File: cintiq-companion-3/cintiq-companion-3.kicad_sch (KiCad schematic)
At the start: 8 parts, among them J3 13HD_buttonboard, J4 13HD_fingerpanel, X1 13HD_eDP, X2 13HD_penpanel

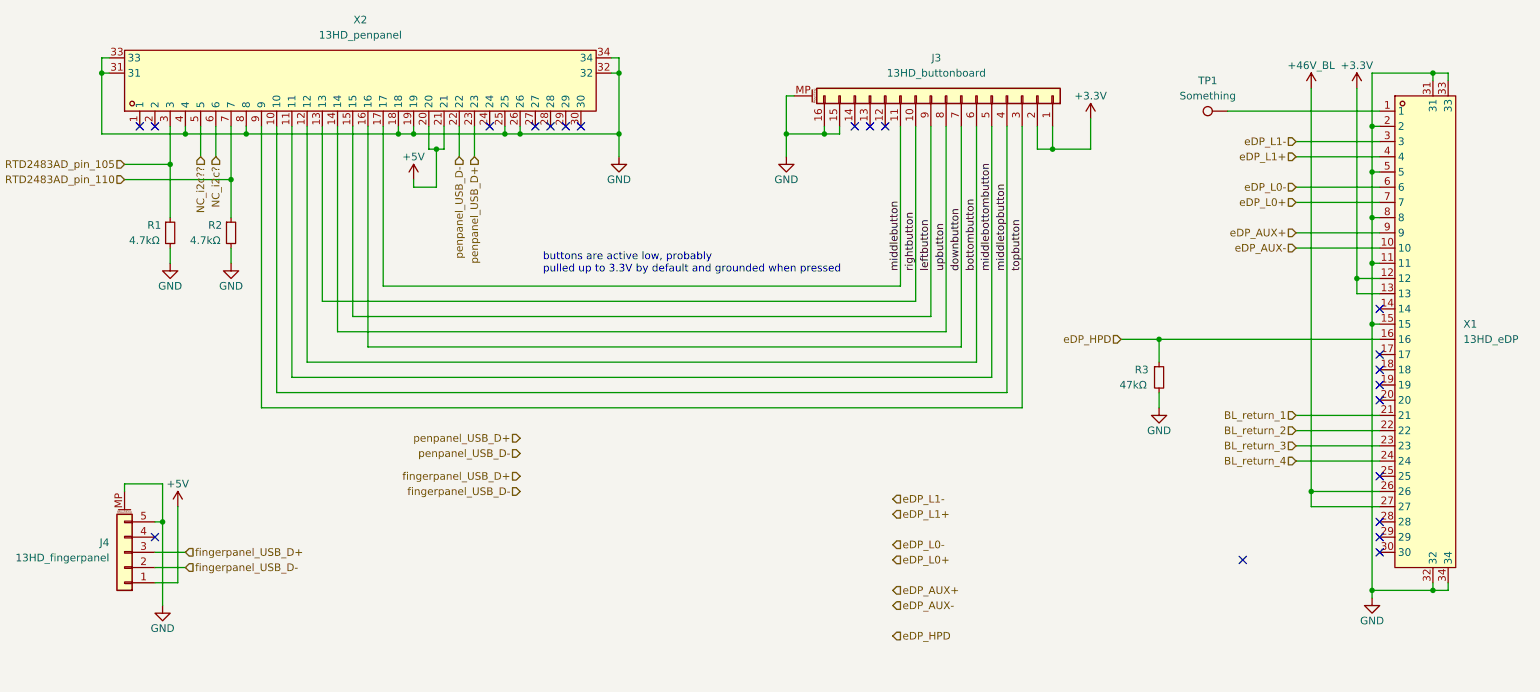
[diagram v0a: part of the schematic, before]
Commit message: Created PCB file with some footprints
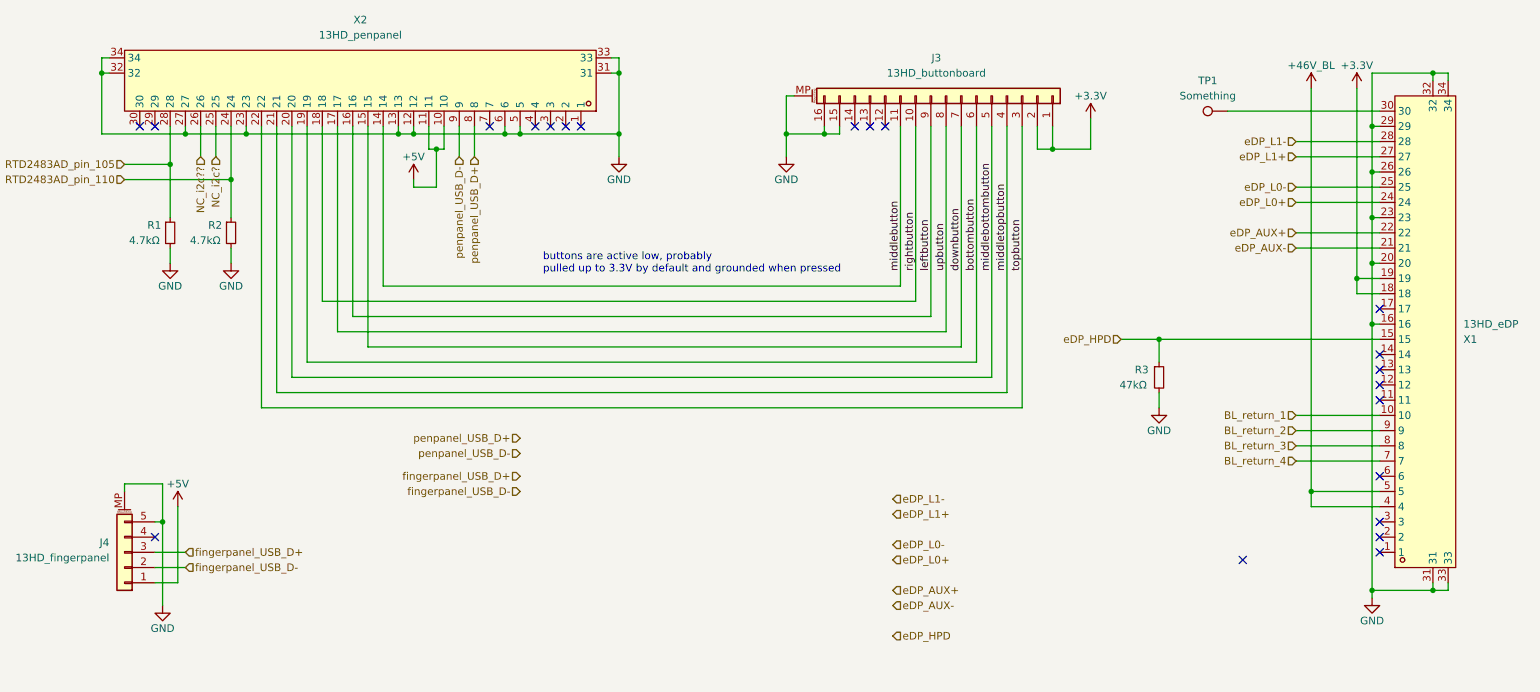
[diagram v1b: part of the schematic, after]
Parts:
- R1, R2, R3: footprint (none) -> Resistor_SMD:R_0603_1608Metric
- X1, X2: footprint 30pipex:FPC-SMD_ALC04-S30EIA-00 -> A_my_stuff:30pipex
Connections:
- net +3.3V: now also X1.18, X1.19; no longer X1.12, X1.13
- net +46V_BL: now also X1.4, X1.5; no longer X1.26, X1.27
- net +5V: now also X2.10, X2.11; no longer X2.20, X2.21
- net BL_return_1: now also X1.10; no longer X1.21
- net BL_return_2: now also X1.9; no longer X1.22
- net BL_return_3: now also X1.8; no longer X1.23
- net BL_return_4: now also X1.7; no longer X1.24
- net GND: now also X1.16, X1.20, X1.23, X1.26, X1.29, X2.12, X2.13, X2.23, X2.27, X2.5, X2.6; no longer X1.11, X1.15, X1.2, X1.5, X1.8, X2.18, X2.19, X2.25, X2.26, X2.4, X2.8
- net NC_i2c?: now also X2.25; no longer X2.6
- net NC_i2c??: now also X2.26; no longer X2.5
- net RTD2483AD_pin_105: now also X2.28; no longer X2.3
- net RTD2483AD_pin_110: now also X2.24; no longer X2.7
- net bottombutton: now also X2.19; no longer X2.12
- net downbutton: now also X2.15; no longer X2.16
- net eDP_AUX+: now also X1.22; no longer X1.9
- net eDP_AUX-: now also X1.21; no longer X1.10
- net eDP_HPD: now also X1.15; no longer X1.16
- net eDP_L0+: now also X1.24; no longer X1.7
- net eDP_L0-: now also X1.25; no longer X1.6
- net eDP_L1+: now also X1.27; no longer X1.4
- net eDP_L1-: now also X1.28; no longer X1.3
- net leftbutton: now also X2.16; no longer X2.15
- net middlebottombutton: now also X2.20; no longer X2.11
- net middlebutton: now also X2.14; no longer X2.17
- net middletopbutton: now also X2.21; no longer X2.10
- net penpanel_USB_D+: now also X2.8; no longer X2.23
- net penpanel_USB_D-: now also X2.9; no longer X2.22
- net rightbutton: now also X2.18; no longer X2.13
- net topbutton: now also X2.22; no longer X2.9
- net upbutton: now also X2.17; no longer X2.14
- net at X1.1: no longer TP1.1
- net at X1.30: now also TP1.1
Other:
- moved on the sheet: X2
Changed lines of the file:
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@@
 			)
 		)
-		(property "Footprint" ""
+		(property "Footprint" "Resistor_SMD:R_0603_1608Metric"
 			(at 213.36 73.66 0)
 			(effects
@@
 			)
 		)
-		(property "Footprint" ""
+		(property "Footprint" "Resistor_SMD:R_0603_1608Metric"
 			(at 58.42 49.53 0)
 			(effects
@@
 			)
 		)
-		(property "Footprint" ""
+		(property "Footprint" "Resistor_SMD:R_0603_1608Metric"
 			(at 48.26 49.53 0)
 			(effects
@@
 		(lib_id "A_my_stuff:30pipex")
 		(at 255.27 66.04 0)
-		(unit 1)
-		(exclude_from_sim no)
-		(in_bom yes)
-		(on_board yes)
-		(dnp no)
-		(fields_autoplaced yes)
+		(mirror x)
+		(unit 1)
+		(exclude_from_sim no)
+		(in_bom yes)
+		(on_board yes)
+		(dnp no)
 		(property "Reference" "X1"
-			(at 264.16 64.7699 0)
+			(at 264.16 67.3101 0)
 			(effects
 				(font
@@
 		)
 		(property "Value" "13HD_eDP"
-			(at 264.16 67.3099 0)
+			(at 264.16 64.7701 0)
 			(effects
 				(font
@@
 			)
 		)
-		(property "Footprint" "30pipex:FPC-SMD_ALC04-S30EIA-00"
-			(at 255.27 115.57 0)
+		(property "Footprint" "A_my_stuff:30pipex"
+			(at 255.27 16.51 0)
 			(effects
 				(font
@@
 		)
 		(property "LCSC Part" "C2842535"
-			(at 255.27 118.11 0)
+			(at 255.27 13.97 0)
 			(effects
 				(font
@@
 	(symbol
 		(lib_id "A_my_stuff:30pipex")
-		(at 80.01 26.67 90)
-		(unit 1)
-		(exclude_from_sim no)
-		(in_bom yes)
-		(on_board yes)
-		(dnp no)
-		(fields_autoplaced yes)
+		(at 80.01 26.67 270)
+		(mirror x)
+		(unit 1)
+		(exclude_from_sim no)
+		(in_bom yes)
+		(on_board yes)
+		(dnp no)
 		(property "Reference" "X2"
 			(at 80.01 13.97 90)
@@
 			)
 		)
-		(property "Footprint" "30pipex:FPC-SMD_ALC04-S30EIA-00"
-			(at 129.54 26.67 0)
+		(property "Footprint" "A_my_stuff:30pipex"
+			(at 30.48 26.67 0)
 			(effects
 				(font
@@
 		)
 		(property "LCSC Part" "C2842535"
-			(at 132.08 26.67 0)
-			(effects
-				(font
+			(at 27.94 26.67 0)
+			(effects
+				(font

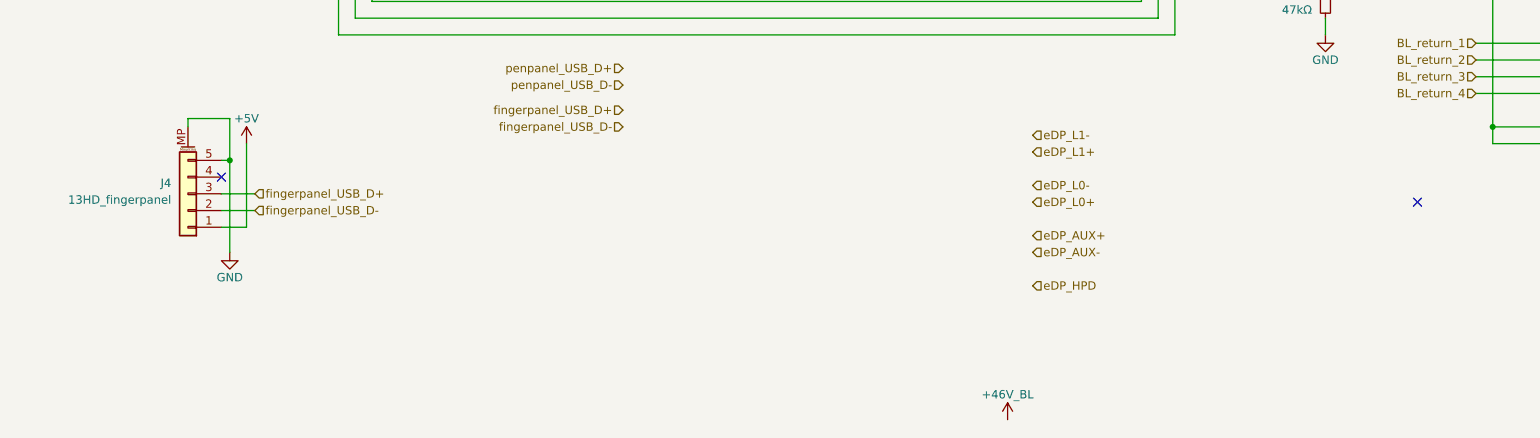
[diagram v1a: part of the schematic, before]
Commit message: Added touch panel USB footprint
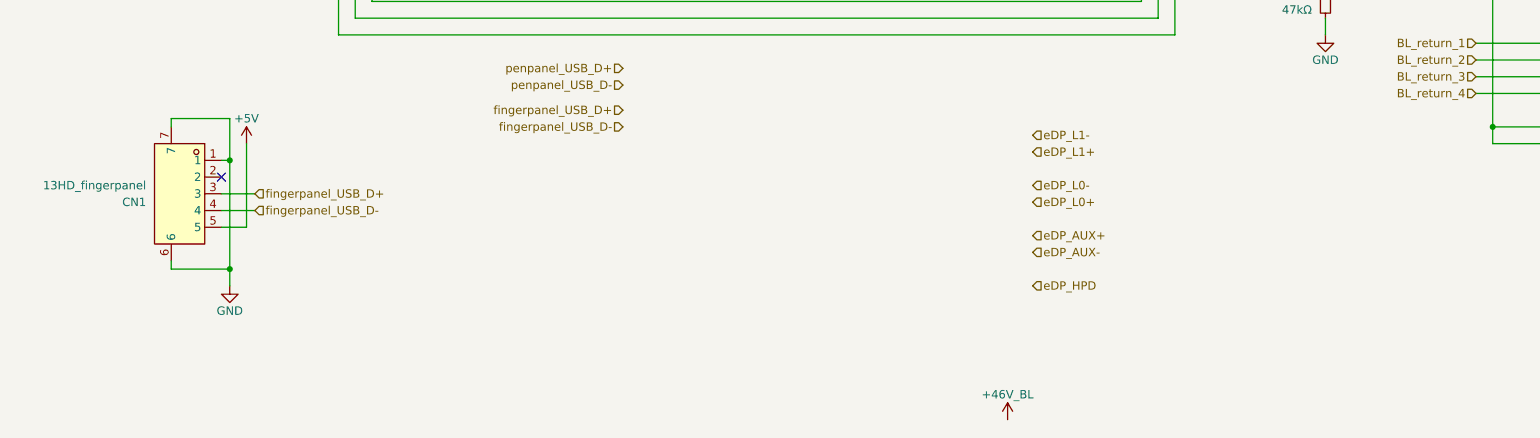
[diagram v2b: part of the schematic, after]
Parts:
- removed J4: 13HD_fingerpanel, symbol Connector_Generic_MountingPin:Conn_01x05_MountingPin
- added CN1: 13HD_fingerpanel, A_my_stuff:minitek5p0.8mm, symbol A_my_stuff:minitek5p0.8mm
- TP1: footprint (none) -> TestPoint:TestPoint_THTPad_D1.5mm_Drill0.7mm
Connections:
- net +5V: now also CN1.5
- net GND: now also CN1.1, CN1.6, CN1.7
- net fingerpanel_USB_D+: now also CN1.3
- net fingerpanel_USB_D-: now also CN1.4
- no-connect marks 21 -> 20
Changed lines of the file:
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@@
 	)
 	(junction
+		(at 46.99 114.3)
+		(diameter 0)
+		(color 0 0 0 0)
+	)
+	(junction
 		(at 248.92 31.75)
 		(diameter 0)
@@
 	)
 	(no_connect
-		(at 227.33 104.14)
-	)
-	(no_connect
 		(at 43.18 31.75)
 	)
@@
 	(wire
 		(pts
+			(xy 38.1 113.03) (xy 38.1 114.3)
+		)
+		(stroke
+			(width 0)
+			(type default)
+		)
+	)
+	(wire
+		(pts
 			(xy 213.36 78.74) (xy 213.36 76.2)
 		)
@@
 	(wire
 		(pts
+			(xy 38.1 91.44) (xy 46.99 91.44)
+		)
+		(stroke
+			(width 0)
+			(type default)
+		)
+	)
+	(wire
+		(pts
 			(xy 248.92 31.75) (xy 248.92 39.37)
 		)
@@
 	(wire
 		(pts
+			(xy 38.1 114.3) (xy 46.99 114.3)
+		)
+		(stroke
+			(width 0)
+			(type default)
+		)
+	)
+	(wire
+		(pts
 			(xy 236.22 85.09) (xy 250.19 85.09)
 		)
@@
 	(wire
 		(pts
+			(xy 38.1 91.44) (xy 38.1 92.71)
+		)
+		(stroke
+			(width 0)
+			(type default)
+		)
+	)
+	(wire
+		(pts
 			(xy 66.04 76.2) (xy 66.04 31.75)
 		)
@@
 	(wire
 		(pts
-			(xy 46.99 91.44) (xy 40.64 91.44)
-		)
-		(stroke
-			(width 0)
-			(type default)
-		)
-	)
-	(wire
-		(pts
 			(xy 123.19 36.83) (xy 123.19 33.02)
 		)
@@
 	(wire
 		(pts
-			(xy 40.64 92.71) (xy 40.64 91.44)
-		)
-		(stroke
-			(width 0)
-			(type default)
-		)
-	)
-	(wire
-		(pts
 			(xy 104.14 33.02) (xy 106.68 33.02)
 		)
@@
 	(wire
 		(pts
-			(xy 46.99 111.76) (xy 46.99 97.79)
+			(xy 46.99 97.79) (xy 46.99 114.3)
 		)
 		(stroke
@@
 	(wire
 		(pts
+			(xy 46.99 116.84) (xy 46.99 114.3)
+		)
+		(stroke
+			(width 0)
+			(type default)
+		)
+	)
+	(wire
+		(pts
 			(xy 88.9 40.64) (xy 88.9 41.91)
 		)
@@
 	(symbol
 		(lib_id "power:GND")
-		(at 46.99 111.76 0)
+		(at 46.99 116.84 0)
 		(unit 1)
 		(exclude_from_sim no)
@@
 		(dnp no)
 		(property "Reference" "#PWR01"
-			(at 46.99 118.11 0)
+			(at 46.99 123.19 0)
 			(effects
 				(font
@@
 		)
 		(property "Value" "GND"
-			(at 46.99 115.57 0)
+			(at 46.99 120.65 0)
 			(effects
 				(font
@@
 		)
 		(property "Footprint" ""
-			(at 46.99 111.76 0)
+			(at 46.99 116.84 0)
 			(effects
 				(font
@@
 		)
 		(property "Datasheet" ""
-			(at 46.99 111.76 0)
+			(at 46.99 116.84 0)
 			(effects
 				(font
@@
 		)
 		(property "Description" "Power symbol creates a global label with name \"GND\" , ground"
-			(at 46.99 111.76 0)
+			(at 46.99 116.84 0)
 			(effects
 				(font
@@
 	)
 	(symbol
-		(lib_id "Connector_Generic_MountingPin:Conn_01x05_MountingPin")
-		(at 40.64 102.87 180)
+		(lib_id "power:GND")
+		(at 248.92 110.49 0)
 		(unit 1)
 		(exclude_from_sim no)
@@
 		(on_board yes)
 		(dnp no)
-		(fields_autoplaced yes)
-		(property "Reference" "J4"
-			(at 38.1 101.2443 0)
+		(property "Reference" "#PWR04"
+			(at 248.92 116.84 0)
 			(effects
 				(font
 					(size 1.27 1.27)
 				)
-				(justify left)
+				(hide yes)
 			)
 		)
-		(property "Value" "13HD_fingerpanel"
-			(at 38.1 103.7843 0)
+		(property "Value" "GND"
+			(at 248.92 114.3 0)
 			(effects
 				(font
 					(size 1.27 1.27)
 				)
-				(justify left)
 			)
 		)
 		(property "Footprint" ""
-			(at 40.64 102.87 0)
+			(at 248.92 110.49 0)
 			(effects
 				(font
@@
 			)
 		)
-		(property "Datasheet" "~"
-			(at 40.64 102.87 0)
+		(property "Datasheet" ""
+			(at 248.92 110.49 0)
 			(effects
 				(font
@@
 			)
 		)
-		(property "Description" "Generic connectable mounting pin connector, single row, 01x05, script generated (kicad-library-utils/schlib/autogen/connector/)"
-			(at 40.64 102.87 0)
+		(property "Description" "Power symbol creates a global label with name \"GND\" , ground"
+			(at 248.92 110.49 0)
 			(effects
 				(font
@@
 			)
 		)
-		(pin "MP"
-		)
-		(pin "4"
-		)
-		(pin "2"
-		)
-		(pin "3"
-		)
-		(pin "5"
-		)
 		(pin "1"
 		)
@@
 			(project "cintiq-companion-3"
 				(path "/ef92970f-f7a1-4011-9c13-6d46a45b923d"
-					(reference "J4")
+					(reference "#PWR04")
 					(unit 1)
 				)
@@
 	)
 	(symbol
-		(lib_id "power:GND")
-		(at 248.92 110.49 0)
+		(lib_id "power:+5V")
+		(at 88.9 40.64 0)
 		(unit 1)
 		(exclude_from_sim no)
@@
 		(on_board yes)
 		(dnp no)
-		(property "Reference" "#PWR04"
-			(at 248.92 116.84 0)
+		(property "Reference" "#PWR06"
+			(at 88.9 44.45 0)
 			(effects
 				(font
@@
 			)
 		)
-		(property "Value" "GND"
-			(at 248.92 114.3 0)
+		(property "Value" "+5V"
+			(at 88.9 36.83 0)
 			(effects
 				(font
@@
 		)
 		(property "Footprint" ""
-			(at 248.92 110.49 0)
+			(at 88.9 40.64 0)
 			(effects
 				(font
@@
 		)
 		(property "Datasheet" ""
-			(at 248.92 110.49 0)
+			(at 88.9 40.64 0)
 			(effects
 				(font
@@
 			)
 		)
-		(property "Description" "Power symbol creates a global label with name \"GND\" , ground"
-			(at 248.92 110.49 0)
+		(property "Description" "Power symbol creates a global label with name \"+5V\""
+			(at 88.9 40.64 0)
 			(effects
 				(font
@@
 			(project "cintiq-companion-3"
 				(path "/ef92970f-f7a1-4011-9c13-6d46a45b923d"
-					(reference "#PWR04")
+					(reference "#PWR06")
 					(unit 1)
 				)
@@
 	)
 	(symbol
-		(lib_id "power:+5V")
-		(at 88.9 40.64 0)
+		(lib_id "A_my_stuff:minitek5p0.8mm")
+		(at 40.64 102.87 0)
+		(mirror y)
 		(unit 1)
 		(exclude_from_sim no)
@@
 		(on_board yes)
 		(dnp no)
-		(property "Reference" "#PWR06"
-			(at 88.9 44.45 0)
+		(property "Reference" "CN1"
+			(at 34.29 104.1401 0)
 			(effects
 				(font
 					(size 1.27 1.27)
 				)
-				(hide yes)
+				(justify left)
 			)
 		)
-		(property "Value" "+5V"
-			(at 88.9 36.83 0)
+		(property "Value" "13HD_fingerpanel"
+			(at 34.29 101.6001 0)
 			(effects
 				(font
 					(size 1.27 1.27)
 				)
+				(justify left)
 			)
 		)
-		(property "Footprint" ""
-			(at 88.9 40.64 0)
+		(property "Footprint" "A_my_stuff:minitek5p0.8mm"
+			(at 40.64 120.65 0)
 			(effects
 				(font
@@
 		)
 		(property "Datasheet" ""
-			(at 88.9 40.64 0)
+			(at 40.64 102.87 0)
 			(effects
 				(font
@@
 			)
 		)
-		(property "Description" "Power symbol creates a global label with name \"+5V\""
-			(at 88.9 40.64 0)
+		(property "Description" ""
+			(at 40.64 102.87 0)
+			(effects
+				(font
+					(size 1.27 1.27)
+				)
+				(hide yes)
+			)
+		)
+		(property "LCSC Part" "C2845346"
+			(at 40.64 123.19 0)
 			(effects
 				(font
@@
 		(pin "1"
 		)
+		(pin "7"
+		)
+		(pin "6"
+		)
+		(pin "2"
+		)
+		(pin "3"
+		)
+		(pin "5"
+		)
+		(pin "4"
+		)
 		(instances
 			(project "cintiq-companion-3"
 				(path "/ef92970f-f7a1-4011-9c13-6d46a45b923d"
-					(reference "#PWR06")
+					(reference "CN1")
 					(unit 1)
 				)
@@
 			)
 		)
-		(property "Footprint" ""
+		(property "Footprint" "TestPoint:TestPoint_THTPad_D1.5mm_Drill0.7mm"
 			(at 224.79 24.13 0)
 			(effects
